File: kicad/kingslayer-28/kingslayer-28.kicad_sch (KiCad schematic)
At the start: 57 parts, among them K1 KEYSW, K10 KEYSW, K11 KEYSW, K12 KEYSW, K13 KEYSW, K14 KEYSW, K15 KEYSW, K16 KEYSW, K17 KEYSW, K18 KEYSW, K19 KEYSW, K2 KEYSW, K20 KEYSW, K21 KEYSW, K22 KEYSW, K23 KEYSW, K24 KEYSW, K25 KEYSW, K26 KEYSW, K27 KEYSW, K28 KEYSW, K3 KEYSW, K4 KEYSW, K5 KEYSW, K6 KEYSW, K7 KEYSW, K8 KEYSW, K9 KEYSW, U1 STM32F303CCTx

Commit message: Setting up microcontroller
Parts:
- removed D1, D10, D11, D12, D13, D14, D15, D16, D17, D18, D19, D2, D20, D21, D22, D23, D24, D25, D26, D27, D28, D3, D4, D5, D6, D7, D8, D9: D, symbol Device:D
- removed U1: STM32F303CCTx, Package_QFP:LQFP-48_7x7mm_P0.5mm, symbol MCU_ST_STM32F3:STM32F303CCTx
- added C1, C2: 22p, symbol Device:C_Small
- added C3, C4, C5, C6: 0.1u, symbol Device:C_Small
- added C7: 4.7u, symbol Device:C_Small
- added D1, D10, D11, D12, D13, D14, D15, D16, D17, D18, D19, D2, D20, D21, D22, D23, D24, D25, D26, D27, D28, D3, D4, D5, D6, D7, D8, D9: D, symbol keyboard_parts:D
- added IC1: STM32F303CCT7, QFP50P900X900X160-48N, symbol STM32F303CCT7:STM32F303CCT7
- added R1: 10k, symbol Device:R
- added SW1: SW_PUSH, symbol keyboard_parts:SW_PUSH
- added X1: XTAL_GND, symbol keyboard_parts:XTAL_GND
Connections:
- net col0: now also IC1.29 (PA8)
- net col1: now also IC1.28 (PB15)
- net col2: now also IC1.27 (PB14)
- net col3: now also IC1.26 (PB13)
- net col4: now also IC1.25 (PB12)
- net col5: now also IC1.38 (PA15)
- net col6: now also IC1.37 (PA14)
- net row0: now also D1.1, D2.1, D3.1, D4.1, D5.1, D6.1, D7.1, IC1.34 (PA13)
- net row1: now also D10.1, D11.1, D12.1, D8.1, D9.1, IC1.33 (PA12)
- net row2: now also D13.1, D14.1, D15.1, D16.1, D17.1, IC1.32 (PA11)
- net row3: now also D18.1, D19.1, D20.1, D21.1, D22.1, D23.1, IC1.31 (PA10)
- net row4: now also D24.1, D25.1, D26.1, D27.1, D28.1, IC1.30 (PA9)
- net at K15.2: now also D15.2
- net at K12.2: now also D8.2
- net at K7.2: now also D7.2
- net at K17.2: now also D17.2
- net at K9.2: now also D11.2
- net at K1.2: now also D1.2
- net at K18.2: now also D22.2
- net at K13.2: now also D13.2
- net at K19.2: now also D21.2
- net at K20.2: now also D20.2
- net at K3.2: now also D3.2
- net at K5.2: now also D5.2
- net at K11.2: now also D9.2
- net at K14.2: now also D14.2
- net at K16.2: now also D16.2
- net at K21.2: now also D19.2
- net at K22.2: now also D18.2
- net at K2.2: now also D2.2
- net at K8.2: now also D12.2
- net at K4.2: now also D4.2
- net at K10.2: now also D10.2
- net at K23.2: now also D23.2
- net at K6.2: now also D6.2
- new net: C1.1, IC1.5 (PF0/OSC_IN), X1.1
- new net: C2.1, IC1.6 (PF1/OSC_OUT), X1.2
- new net: IC1.7 (NRST), R1.2, SW1.2
- new net +5V: C1.2, C2.2, C3.2, C4.2, C5.2, C6.2, C7.2, IC1.23 (VSS_1), IC1.35 (VSS_2), IC1.47 (VSS_3), IC1.8 (VSSA/VREF-), SW1.1, X1.3
- new net VCC: C3.1, C4.1, C5.1, C6.1, C7.1, IC1.1 (VBAT), IC1.24 (VDD_1), IC1.36 (VDD_2), IC1.48 (VDD_3), IC1.9 (VDDA), R1.1
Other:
- moved on the sheet: K10, K11, K12, K13, K14, K15, K16, K17, K18, K20, K21, K22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

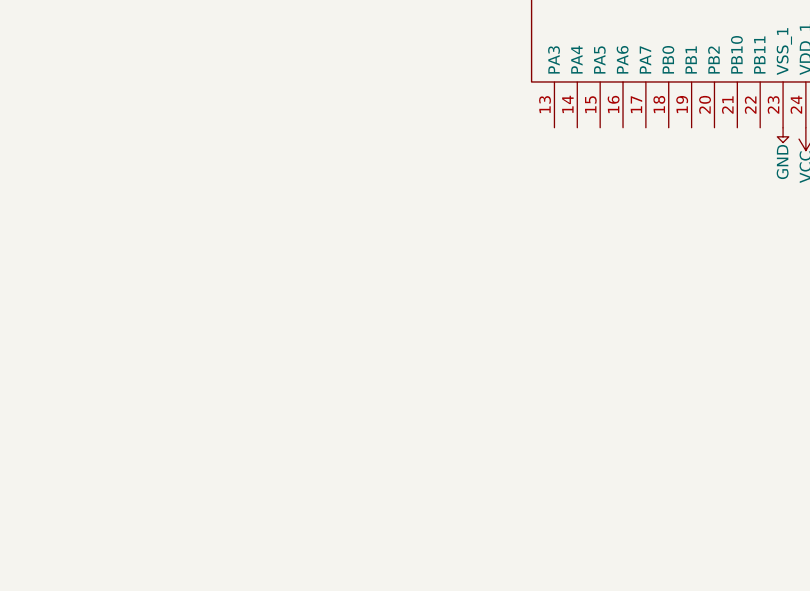
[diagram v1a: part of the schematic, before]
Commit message: Add RGB controller
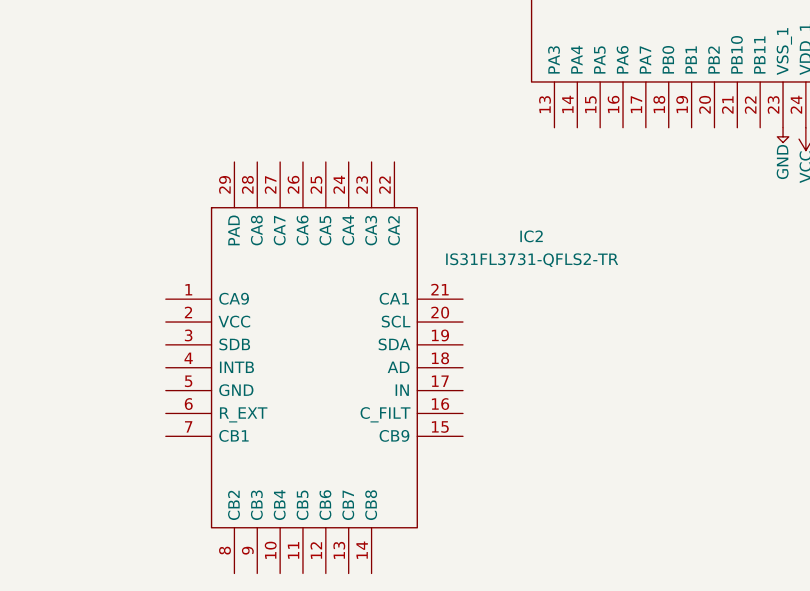
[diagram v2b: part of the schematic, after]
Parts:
- added IC2: IS31FL3731-QFLS2-TR, QFN40P400X400X80-29N, symbol IS31FL3731-QFLS2-TR:IS31FL3731-QFLS2-TR
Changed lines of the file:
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@@
+    )
+  )
+  (symbol (lib_id "IS31FL3731-QFLS2-TR:IS31FL3731-QFLS2-TR") (at 190.5 113.03 0) (unit 1)
+    (in_bom yes) (on_board yes) (dnp no) (fields_autoplaced)
+    (property "Reference" "IC2" (at 231.14 106.1019 0)
+      (effects (font (size 1.27 1.27)))
+    )
+    (property "Value" "IS31FL3731-QFLS2-TR" (at 231.14 108.6419 0)
+      (effects (font (size 1.27 1.27)))
+    )
+    (property "Footprint" "QFN40P400X400X80-29N" (at 219.71 102.87 0)
+      (effects (font (size 1.27 1.27)) (justify left) hide)
+    )
+    (property "Datasheet" "https://componentsearchengine.com/Datasheets/1/IS31FL3731-QFLS2-TR.pdf" (at 219.71 105.41 0)
+      (effects (font (size 1.27 1.27)) (justify left) hide)
+    )
+    (property "Description" "LED Lighting Drivers LED Driver" (at 219.71 107.95 0)
+      (effects (font (size 1.27 1.27)) (justify left) hide)
+    )
+    (property "Height" "0.8" (at 219.71 110.49 0)
+      (effects (font (size 1.27 1.27)) (justify left) hide)
+    )
+    (property "Mouser Part Number" "870-31FL3731-QFLS2TR" (at 219.71 113.03 0)
+      (effects (font (size 1.27 1.27)) (justify left) hide)
+    )
+    (property "Mouser Price/Stock" "https://www.mouser.com/Search/Refine.aspx?Keyword=870-31FL3731-QFLS2TR" (at 219.71 115.57 0)
+      (effects (font (size 1.27 1.27)) (justify left) hide)
+    )
+    (property "Manufacturer_Name" "Integrated Silicon Solution Inc." (at 219.71 118.11 0)
+      (effects (font (size 1.27 1.27)) (justify left) hide)
+    )
+    (property "Manufacturer_Part_Number" "IS31FL3731-QFLS2-TR" (at 219.71 120.65 0)
+      (effects (font (size 1.27 1.27)) (justify left) hide)
+    )
+    (pin "1")
+    (pin "10")
+    (pin "11")
+    (pin "12")
+    (pin "13")
+    (pin "14")
+    (pin "15")
+    (pin "16")
+    (pin "17")
+    (pin "18")
+    (pin "19")
+    (pin "2")
+    (pin "20")
+    (pin "21")
+    (pin "22")
+    (pin "23")
+    (pin "24")
+    (pin "25")
+    (pin "26")
+    (pin "27")
+    (pin "28")
+    (pin "29")
+    (pin "3")
+    (pin "4")
+    (pin "5")
+    (pin "6")
+    (pin "7")
+    (pin "8")
+    (pin "9")
+    (instances
+      (project "kingslayer-28"
+        (path "/7c3679ab-fb1a-4578-bd30-c0b9ef7b8f3d"
+          (reference "IC2") (unit 1)
+        )
+      )
     )
   )

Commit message: tidy up the schematic
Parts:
- added D29: LED_BRAG, symbol Device:LED_BRAG
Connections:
- net xtal1: now reaches C1.1, IC1.5 (PF0/OSC_IN), X1.1
- net xtal2: now reaches C2.1, IC1.6 (PF1/OSC_OUT), X1.2
- net nrst: now reaches IC1.7 (NRST), R1.2, SW1.2
- net at K26.2: now also D26.2
- net at D28.2: now also K28.2
- net at D24.2: now also K24.2
- net at D25.2: now also K25.2
- net at K27.2: now also D27.2
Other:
- moved on the sheet: C1, C2, C3, C4, C5, C6, C7, D1, D10, D11, D12, D13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

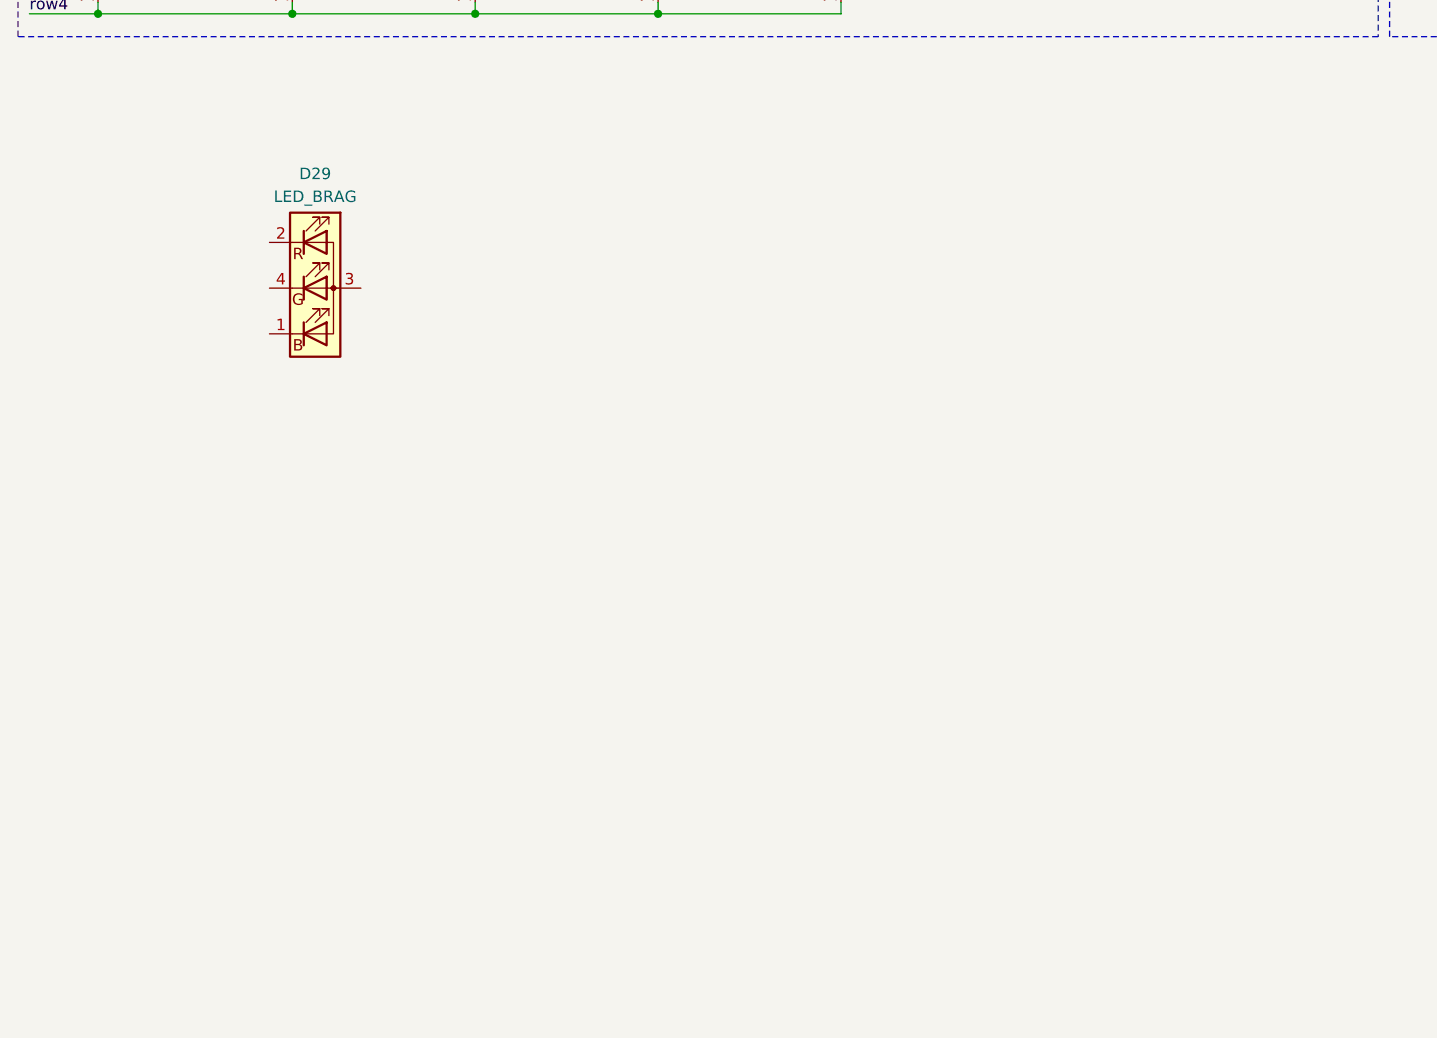
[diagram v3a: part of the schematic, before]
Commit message: add RGB matrix
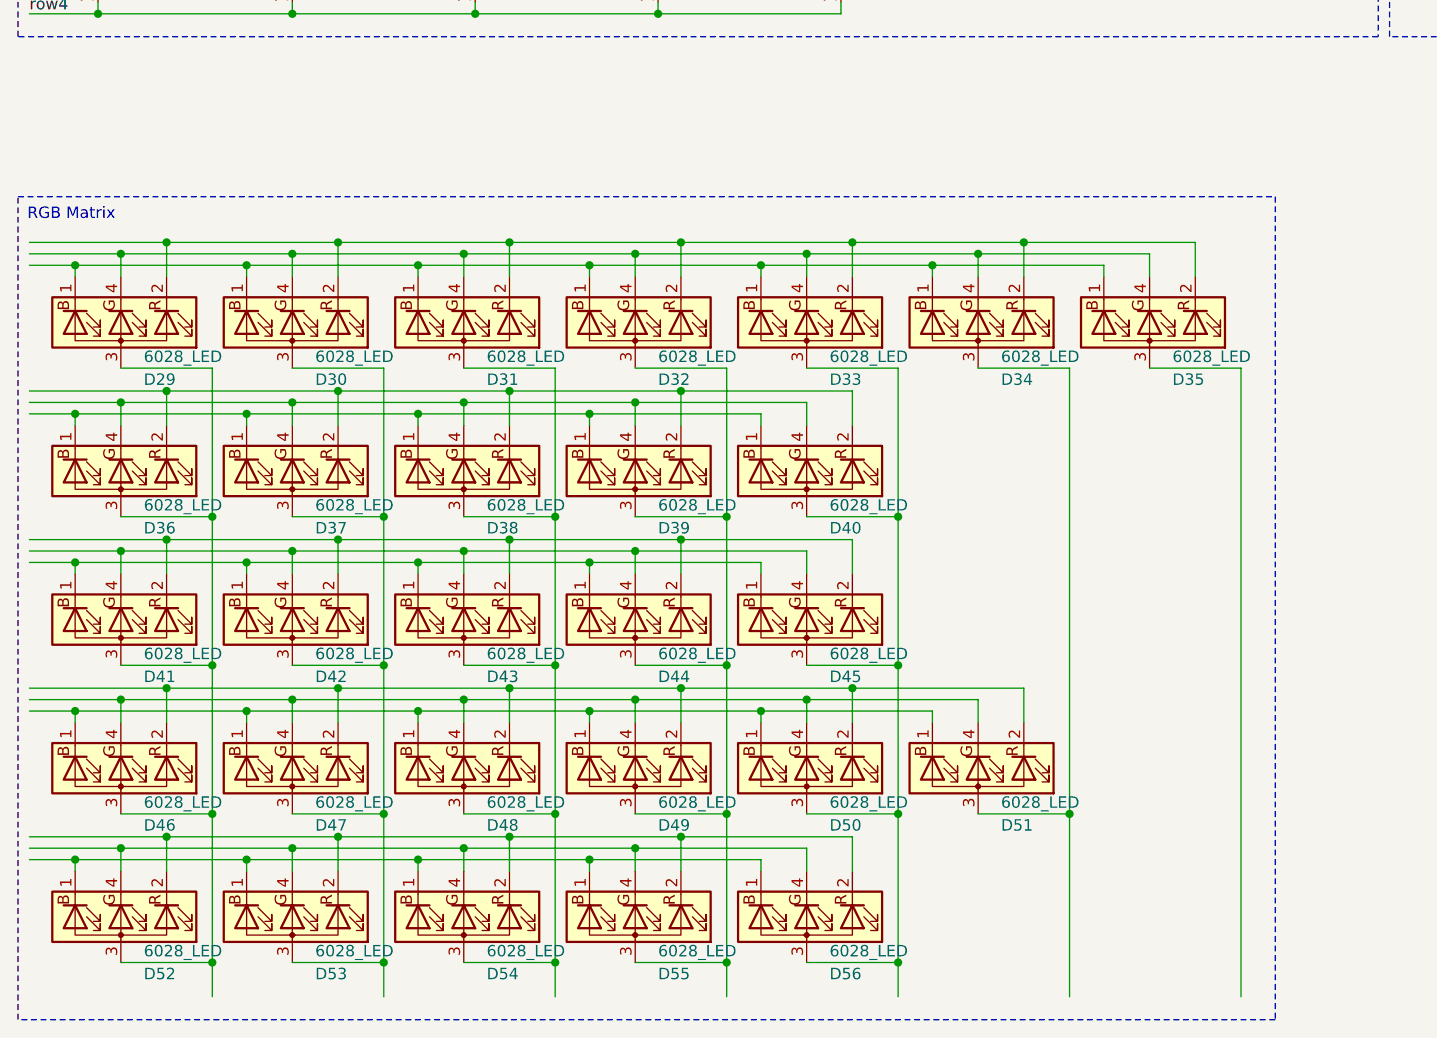
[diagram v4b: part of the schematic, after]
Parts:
- added D30, D31, D32, D33, D34, D35, D36, D37, D38, D39, D40, D41, D42, D43, D44, D45, D46, D47, D48, D49, D50, D51, D52, D53, D54, D55, D56: 6028_LED, symbol Device:LED_BRAG
- D29: value LED_BRAG -> 6028_LED
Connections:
- net at D29.1 (BK): now also D30.1 (BK), D31.1 (BK), D32.1 (BK), D33.1 (BK), D34.1 (BK), D35.1 (BK)
- net at D29.2 (RK): now also D30.2 (RK), D31.2 (RK), D32.2 (RK), D33.2 (RK), D34.2 (RK), D35.2 (RK)
- net at D29.3 (A): now also D36.3 (A), D41.3 (A), D46.3 (A), D52.3 (A)
- net at D29.4 (GK): now also D30.4 (GK), D31.4 (GK), D32.4 (GK), D33.4 (GK), D34.4 (GK), D35.4 (GK)
- new net: D30.3 (A), D37.3 (A), D42.3 (A), D47.3 (A), D53.3 (A)
- new net: D36.1 (BK), D37.1 (BK), D38.1 (BK), D39.1 (BK), D40.1 (BK)
- new net: D36.2 (RK), D37.2 (RK), D38.2 (RK), D39.2 (RK), D40.2 (RK)
- new net: D32.3 (A), D39.3 (A), D44.3 (A), D49.3 (A), D55.3 (A)
- new net: D36.4 (GK), D37.4 (GK), D38.4 (GK), D39.4 (GK), D40.4 (GK)
- new net: D52.1 (BK), D53.1 (BK), D54.1 (BK), D55.1 (BK), D56.1 (BK)
- new net: D52.2 (RK), D53.2 (RK), D54.2 (RK), D55.2 (RK), D56.2 (RK)
- new net: D52.4 (GK), D53.4 (GK), D54.4 (GK), D55.4 (GK), D56.4 (GK)
- new net: D46.1 (BK), D47.1 (BK), D48.1 (BK), D49.1 (BK), D50.1 (BK), D51.1 (BK)
- new net: D46.2 (RK), D47.2 (RK), D48.2 (RK), D49.2 (RK), D50.2 (RK), D51.2 (RK)
- new net: D34.3 (A), D51.3 (A)
- new net: D46.4 (GK), D47.4 (GK), D48.4 (GK), D49.4 (GK), D50.4 (GK), D51.4 (GK)
- new net: D41.1 (BK), D42.1 (BK), D43.1 (BK), D44.1 (BK), D45.1 (BK)
- new net: D41.2 (RK), D42.2 (RK), D43.2 (RK), D44.2 (RK), D45.2 (RK)
- new net: D41.4 (GK), D42.4 (GK), D43.4 (GK), D44.4 (GK), D45.4 (GK)
- new net: D33.3 (A), D40.3 (A), D45.3 (A), D50.3 (A), D56.3 (A)
- new net: D31.3 (A), D38.3 (A), D43.3 (A), D48.3 (A), D54.3 (A)
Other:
- moved on the sheet: D29

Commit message: RGB matrix 2
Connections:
- net ca3: now reaches D29.1 (BK), D30.1 (BK), D31.1 (BK), D32.1 (BK), D33.1 (BK), D34.1 (BK)
- net ca3: now also D38.3 (A), D43.3 (A), IC2.23 (CA3); no longer D35.1 (BK)
- net ca1: now reaches D29.2 (RK), D30.2 (RK), D31.2 (RK), D32.2 (RK), D33.2 (RK), D34.2 (RK)
- net ca1: now also D36.3 (A), D41.3 (A), IC2.21 (CA1); no longer D35.2 (RK)
- net cb1: now reaches D35.3 (A)
- net cb1: now also D46.2 (RK), D47.2 (RK), D48.2 (RK), D49.2 (RK), D50.2 (RK), D51.2 (RK), D52.3 (A), IC2.7 (CB1)
- net ca2: now reaches D29.4 (GK), D30.4 (GK), D31.4 (GK), D32.4 (GK), D33.4 (GK), D34.4 (GK)
- net ca2: now also D37.3 (A), D42.3 (A), IC2.22 (CA2); no longer D35.4 (GK)
- net ca6: now reaches D36.1 (BK), D37.1 (BK), D38.1 (BK), D39.1 (BK), D40.1 (BK)
- net ca6: now also D31.3 (A), IC2.26 (CA6)
- net ca4: now reaches D36.2 (RK), D37.2 (RK), D38.2 (RK), D39.2 (RK), D40.2 (RK)
- net ca4: now also D29.3 (A), D44.3 (A), IC2.24 (CA4)
- net ca5: now reaches D36.4 (GK), D37.4 (GK), D38.4 (GK), D39.4 (GK), D40.4 (GK)
- net ca5: now also D30.3 (A), D45.3 (A), IC2.25 (CA5)
- net cb6: now reaches D52.1 (BK), D53.1 (BK), D54.1 (BK), D55.1 (BK), D56.1 (BK)
- net cb6: now also D48.3 (A), IC2.12 (CB6)
- net cb4: now reaches D52.2 (RK), D53.2 (RK), D54.2 (RK), D55.2 (RK), D56.2 (RK)
- net cb4: now also D46.3 (A), IC2.10 (CB4)
- net cb5: now reaches D52.4 (GK), D53.4 (GK), D54.4 (GK), D55.4 (GK), D56.4 (GK)
- net cb5: now also D47.3 (A), IC2.11 (CB5)
- net cb3: now reaches D46.1 (BK), D47.1 (BK), D48.1 (BK), D49.1 (BK), D50.1 (BK), D51.1 (BK)
- net cb3: now also D54.3 (A), IC2.9 (CB3)
- net ca9: now reaches D34.3 (A)
- net ca9: now also D41.1 (BK), D42.1 (BK), D43.1 (BK), D44.1 (BK), D45.1 (BK), IC2.1 (CA9); no longer D51.3 (A)
- net cb2: now reaches D46.4 (GK), D47.4 (GK), D48.4 (GK), D49.4 (GK), D50.4 (GK), D51.4 (GK)
- net cb2: now also D53.3 (A), IC2.8 (CB2)
- net ca7: now reaches D41.2 (RK), D42.2 (RK), D43.2 (RK), D44.2 (RK), D45.2 (RK)
- net ca7: now also D32.3 (A), D39.3 (A), IC2.27 (CA7)
- net ca8: now reaches D41.4 (GK), D42.4 (GK), D43.4 (GK), D44.4 (GK), D45.4 (GK)
- net ca8: now also D33.3 (A), D40.3 (A), IC2.28 (CA8)
- net cb7: now reaches IC2.13 (CB7)
- net cb7: now also D35.2 (RK), D49.3 (A), D55.3 (A)
- net cb8: now reaches IC2.14 (CB8)
- net cb8: now also D35.4 (GK), D50.3 (A), D56.3 (A)
- net cb9: now reaches IC2.15 (CB9)
- net cb9: now also D35.1 (BK), D51.3 (A)

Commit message: USB C
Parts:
- removed D29, D30, D31, D32, D33, D34, D35, D36, D37, D38, D39, D40, D41, D42, D43, D44, D45, D46, D47, D48, D49, D50, D51, D52, D53, D54, D55, D56: 6028_LED, symbol Device:LED_BRAG
- removed IC2: IS31FL3731-QFLS2-TR, QFN40P400X400X80-29N, symbol IS31FL3731-QFLS2-TR:IS31FL3731-QFLS2-TR
- added USB1: 12401598E4#2A, symbol Type-C:12401598E4#2A
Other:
- added sheet RGB (rgb.kicad_sch)
- moved on the sheet: IC1

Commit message: connect rgb
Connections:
- net sda: now reaches IC1.39 (PB3)
- net scl: now reaches IC1.40 (PB4)

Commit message: progress?
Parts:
- removed R1: 10k, symbol Device:R
- removed SW1: SW_PUSH, symbol keyboard_parts:SW_PUSH
- removed X1: XTAL_GND, symbol keyboard_parts:XTAL_GND
- added S1: TL3342F260QG, TL3342F260QG, symbol TL3342F260QG:TL3342F260QG
- added Y1: FA-238_16.0000MB-C3, FA238160000MBC3, symbol FA-238_16.0000MB-C3:FA-238_16.0000MB-C3
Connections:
- net +5V: now also C3.1, C4.1, C5.1, C6.1, C7.1, S1.1, S1.3, Y1.2 (GND_1), Y1.4 (GND_2)
- net VCC: no longer C3.1, C4.1, C5.1, C6.1, C7.1
- net xtal1: now also Y1.1 (CRYSTAL_1)
- net xtal2: now also Y1.3 (CRYSTAL_2)
- net boot0: now reaches IC1.44 (BOOT0)
- new net: S1.2, S1.4
- no-connect marks 0 -> 3
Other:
- note added: "?"
- note added: "This will need to be 8MHZ I think"
- moved on the sheet: C1, C2
